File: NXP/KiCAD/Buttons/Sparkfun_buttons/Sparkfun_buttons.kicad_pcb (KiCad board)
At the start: 2 copper layers, 100 x 70 mm, 25 parts, among them J1 Screw_Terminal_01x12, SW1 15mm_Silicone_Buttons

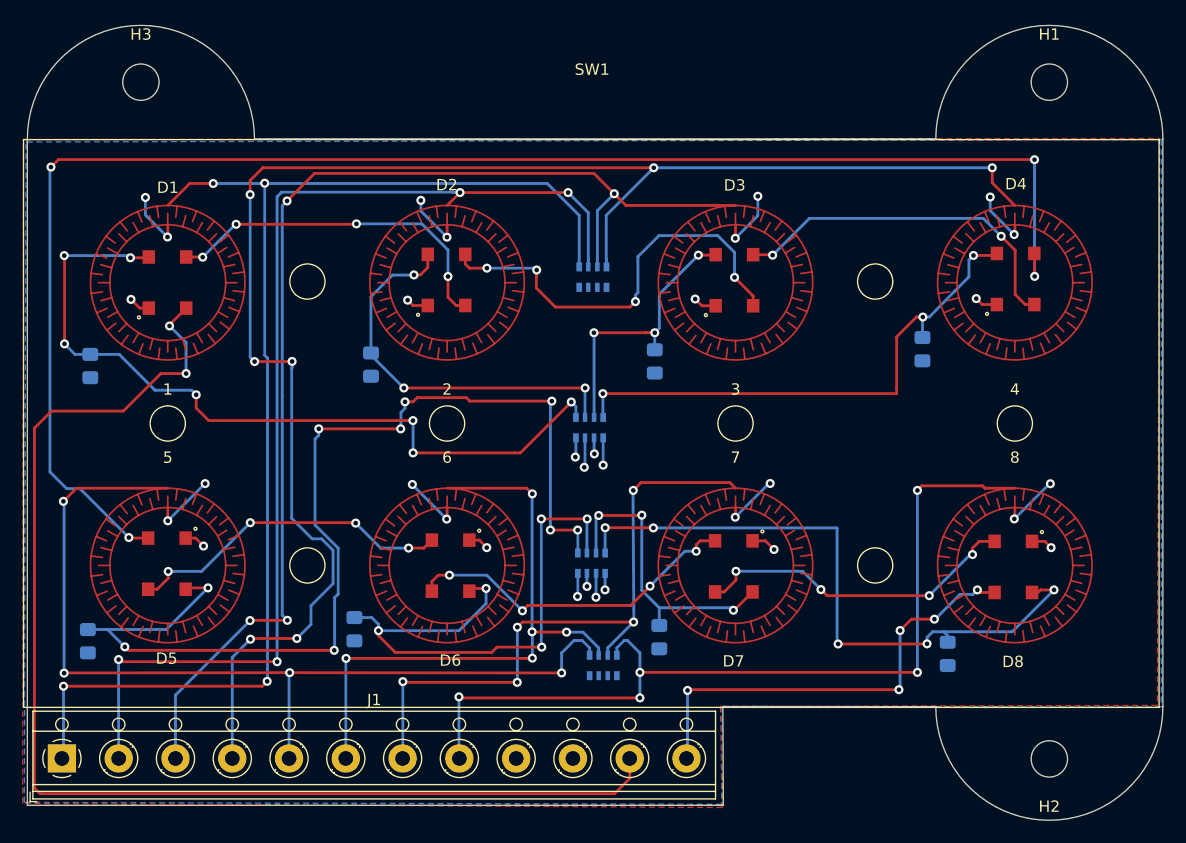
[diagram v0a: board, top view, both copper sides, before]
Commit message: 80% done with the controller. Will have done and ready for review this friday.
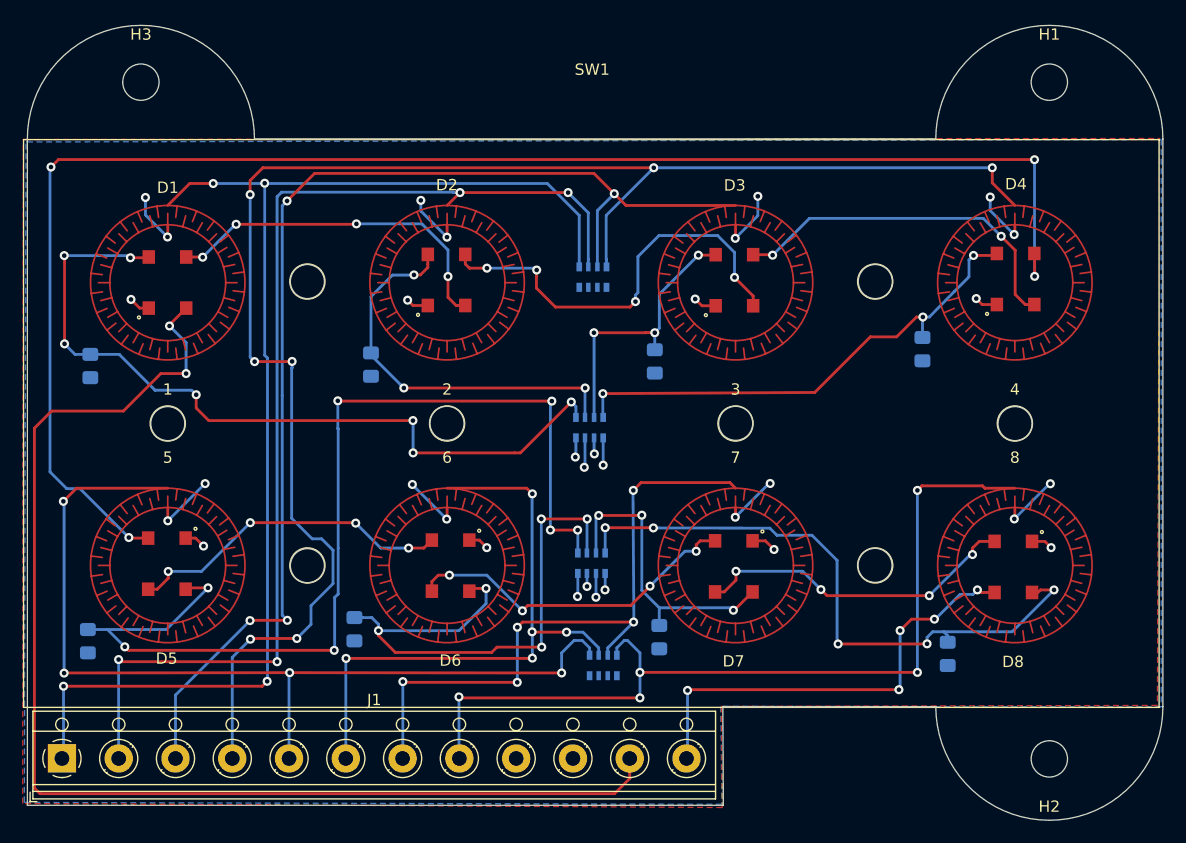
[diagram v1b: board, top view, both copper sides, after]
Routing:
- net Net-(C7-Pad1): track 47.5 -> 44.6 mm
- net Net-(C2-Pad1): track 94.3 -> 91.7 mm, vias 9 -> 7
- net Net-(C8-Pad1): track 56.9 -> 55.3 mm
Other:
- outline, holes or cut-outs redrawn
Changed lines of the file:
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@@
   (general
     (thickness 1.6)
-    (drawings 9)
-    (tracks 610)
+    (drawings 17)
+    (tracks 602)
     (zones 0)
     (modules 25)
@@
     (solder_mask_min_width 0.25)
     (aux_axis_origin 0 0)
-    (visible_elements FFFFFF7F)
+    (visible_elements 7FFFFFFF)
     (pcbplotparams
       (layerselection 0x010fc_ffffffff)
@@
     )
   )
+  (gr_circle (center 154.6479 68.8707) (end 156.1479 68.8707) (layer Edge.Cuts) (width 0.05))
+  (gr_circle (center 166.981 56.388) (end 168.481 56.388) (layer Edge.Cuts) (width 0.05))
+  (gr_circle (center 154.6747 43.8785) (end 156.1747 43.8785) (layer Edge.Cuts) (width 0.05))
+  (gr_circle (center 142.3783 56.3626) (end 143.8783 56.3626) (layer Edge.Cuts) (width 0.05))
+  (gr_circle (center 104.6621 68.8975) (end 106.1621 68.8975) (layer Edge.Cuts) (width 0.05))
+  (gr_circle (center 116.9557 56.3626) (end 118.4557 56.3626) (layer Edge.Cuts) (width 0.05))
+  (gr_circle (center 92.3685 56.388) (end 93.8685 56.388) (layer Edge.Cuts) (width 0.05))
+  (gr_circle (center 104.6607 43.8771) (end 106.1607 43.8771) (layer Edge.Cuts) (width 0.05))
   (gr_line (start 141.2494 81.3182) (end 160 81.3182) (layer Edge.Cuts) (width 0.05))
   (gr_line (start 141.2875 90) (end 141.2494 81.3182) (layer Edge.Cuts) (width 0.05))
@@
   (via (at 126.1872 54.4068) (size 0.8) (drill 0.4) (layers F.Cu B.Cu) (net 3))
   (segment (start 126.0602 54.5338) (end 126.1872 54.4068) (width 0.25) (layer B.Cu) (net 3))
-  (segment (start 126.1872 54.4068) (end 118.9609 54.4068) (width 0.25) (layer F.Cu) (net 3))
-  (segment (start 118.9609 54.4068) (end 118.6561 54.102) (width 0.25) (layer F.Cu) (net 3))
-  (segment (start 118.6561 54.102) (end 114.3381 54.102) (width 0.25) (layer F.Cu) (net 3))
-  (via (at 113.2586 54.4703) (size 0.8) (drill 0.4) (layers F.Cu B.Cu) (net 3))
-  (segment (start 114.3381 54.102) (end 113.9698 54.4703) (width 0.25) (layer F.Cu) (net 3))
-  (segment (start 113.9698 54.4703) (end 113.2586 54.4703) (width 0.25) (layer F.Cu) (net 3))
-  (segment (start 113.2586 55.035985) (end 112.903 55.391585) (width 0.25) (layer B.Cu) (net 3))
-  (segment (start 113.2586 54.4703) (end 113.2586 55.035985) (width 0.25) (layer B.Cu) (net 3))
-  (via (at 112.8776 56.8463) (size 0.8) (drill 0.4) (layers F.Cu B.Cu) (net 3))
-  (segment (start 112.903 55.391585) (end 112.903 56.8209) (width 0.25) (layer B.Cu) (net 3))
-  (segment (start 112.903 56.8209) (end 112.8776 56.8463) (width 0.25) (layer B.Cu) (net 3))
-  (via (at 105.664 56.8463) (size 0.8) (drill 0.4) (layers F.Cu B.Cu) (net 3))
-  (segment (start 112.8776 56.8463) (end 105.664 56.8463) (width 0.25) (layer F.Cu) (net 3))
-  (segment (start 105.664 57.411985) (end 105.3338 57.742185) (width 0.25) (layer B.Cu) (net 3))
-  (segment (start 105.664 56.8463) (end 105.664 57.411985) (width 0.25) (layer B.Cu) (net 3))
-  (segment (start 105.3338 57.742185) (end 105.3338 65.31469) (width 0.25) (layer B.Cu) (net 3))
   (segment (start 107.37131 67.3522) (end 107.37131 71.39389) (width 0.25) (layer B.Cu) (net 3))
-  (segment (start 105.3338 65.31469) (end 107.37131 67.3522) (width 0.25) (layer B.Cu) (net 3))
   (segment (start 107.37131 71.39389) (end 107.061 71.7042) (width 0.25) (layer B.Cu) (net 3))
   (via (at 95.9104 70.8533) (size 0.8) (drill 0.4) (layers F.Cu B.Cu) (net 3))
@@
   (segment (start 92.2401 74.5236) (end 95.9104 70.8533) (width 0.25) (layer B.Cu) (net 3))
   (segment (start 87.0585 74.5236) (end 92.2401 74.5236) (width 0.25) (layer B.Cu) (net 3))
+  (segment (start 107.37131 56.85239) (end 107.3774 56.8463) (width 0.25) (layer B.Cu) (net 3))
+  (segment (start 107.37131 67.3522) (end 107.37131 56.85239) (width 0.25) (layer B.Cu) (net 3))
+  (via (at 107.3404 54.3814) (size 0.8) (drill 0.4) (layers F.Cu B.Cu) (net 3))
+  (segment (start 126.1872 54.4068) (end 107.3658 54.4068) (width 0.25) (layer F.Cu) (net 3))
+  (segment (start 107.3658 54.4068) (end 107.3404 54.3814) (width 0.25) (layer F.Cu) (net 3))
+  (segment (start 107.3404 56.8093) (end 107.3774 56.8463) (width 0.25) (layer B.Cu) (net 3))
+  (segment (start 107.3404 54.3814) (end 107.3404 56.8093) (width 0.25) (layer B.Cu) (net 3))
   (segment (start 115.3287 41.4401) (end 115.3414 41.4274) (width 0.25) (layer F.Cu) (net 4))
   (segment (start 113.157 53.2511) (end 113.157 53.2511) (width 0.25) (layer B.Cu) (net 4))
@@
   (segment (start 163.322 41.5798) (end 165.2016 41.5798) (width 0.25) (layer F.Cu) (net 8))
   (via (at 130.683 53.7464) (size 0.8) (drill 0.4) (layers F.Cu B.Cu) (net 8))
-  (segment (start 130.683 53.7464) (end 156.5529 53.7464) (width 0.25) (layer F.Cu) (net 8))
   (segment (start 158.8262 48.8061) (end 158.8262 47.0408) (width 0.25) (layer B.Cu) (net 8))
   (via (at 158.8643 47.0027) (size 0.8) (drill 0.4) (layers F.Cu B.Cu) (net 8))
   (segment (start 158.8262 47.0408) (end 158.8643 47.0027) (width 0.25) (layer B.Cu) (net 8))
-  (segment (start 156.5529 53.180715) (end 156.5529 53.7464) (width 0.25) (layer F.Cu) (net 8))
-  (segment (start 156.5529 48.748415) (end 156.5529 53.180715) (width 0.25) (layer F.Cu) (net 8))
   (segment (start 158.298615 47.0027) (end 156.5529 48.748415) (width 0.25) (layer F.Cu) (net 8))
   (segment (start 158.8643 47.0027) (end 158.298615 47.0027) (width 0.25) (layer F.Cu) (net 8))
@@
   (segment (start 130.683 55.8167) (end 130.7082 55.8419) (width 0.25) (layer B.Cu) (net 8))
   (segment (start 130.683 53.7464) (end 130.683 55.8167) (width 0.25) (layer B.Cu) (net 8))
+  (segment (start 154.235685 48.748415) (end 149.3393 53.6448) (width 0.25) (layer F.Cu) (net 8))
+  (segment (start 156.5529 48.748415) (end 154.235685 48.748415) (width 0.25) (layer F.Cu) (net 8))
+  (segment (start 130.683 53.7464) (end 149.3393 53.6448) (width 0.25) (layer F.Cu) (net 8))
   (via (at 170.412467 71.033047) (size 0.8) (drill 0.4) (layers F.Cu B.Cu) (net 9))
   (segment (start 169.223553 71.033047) (end 168.8953 71.3613) (width 0.25) (layer F.Cu) (net 9))
@@
   (segment (start 130.8862 65.5574) (end 135.111297 65.5574) (width 0.25) (layer F.Cu) (net 9))
   (segment (start 135.111297 65.5574) (end 135.128739 65.574842) (width 0.25) (layer F.Cu) (net 9))
-  (segment (start 135.128739 65.574842) (end 151.274442 65.574842) (width 0.25) (layer B.Cu) (net 9))
-  (segment (start 151.274442 65.574842) (end 151.3078 65.6082) (width 0.25) (layer B.Cu) (net 9))
   (via (at 151.3967 75.7936) (size 0.8) (drill 0.4) (layers F.Cu B.Cu) (net 9))
-  (segment (start 151.3078 65.6082) (end 151.3078 75.7047) (width 0.25) (layer B.Cu) (net 9))
   (segment (start 151.3078 75.7047) (end 151.3967 75.7936) (width 0.25) (layer B.Cu) (net 9))
   (via (at 159.2326 75.7809) (size 0.8) (drill 0.4) (layers F.Cu B.Cu) (net 9))
@@
   (segment (start 166.725599 74.719915) (end 170.412467 71.033047) (width 0.25) (layer B.Cu) (net 9))
   (segment (start 160.702415 74.719915) (end 166.725599 74.719915) (width 0.25) (layer B.Cu) (net 9))
+  (segment (start 149.102742 66.222542) (end 151.3078 68.4276) (width 0.25) (layer B.Cu) (net 9))
+  (segment (start 151.3078 68.4276) (end 151.3078 75.7047) (width 0.25) (layer B.Cu) (net 9))
+  (segment (start 146.016642 66.222542) (end 145.3896 65.5955) (width 0.25) (layer B.Cu) (net 9))
+  (segment (start 149.102742 66.222542) (end 146.016642 66.222542) (width 0.25) (layer B.Cu) (net 9))
+  (segment (start 135.128739 65.574842) (end 145.3896 65.5955) (width 0.25) (layer B.Cu) (net 9))
   (segment (start 93.9927 41.7153) (end 95.4236 41.7153) (width 0.25) (layer F.Cu) (net 10))
   (via (at 95.4405 41.7322) (size 0.8) (drill 0.4) (layers F.Cu B.Cu) (net 10))
